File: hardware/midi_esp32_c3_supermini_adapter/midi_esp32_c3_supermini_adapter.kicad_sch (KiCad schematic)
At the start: 0 parts

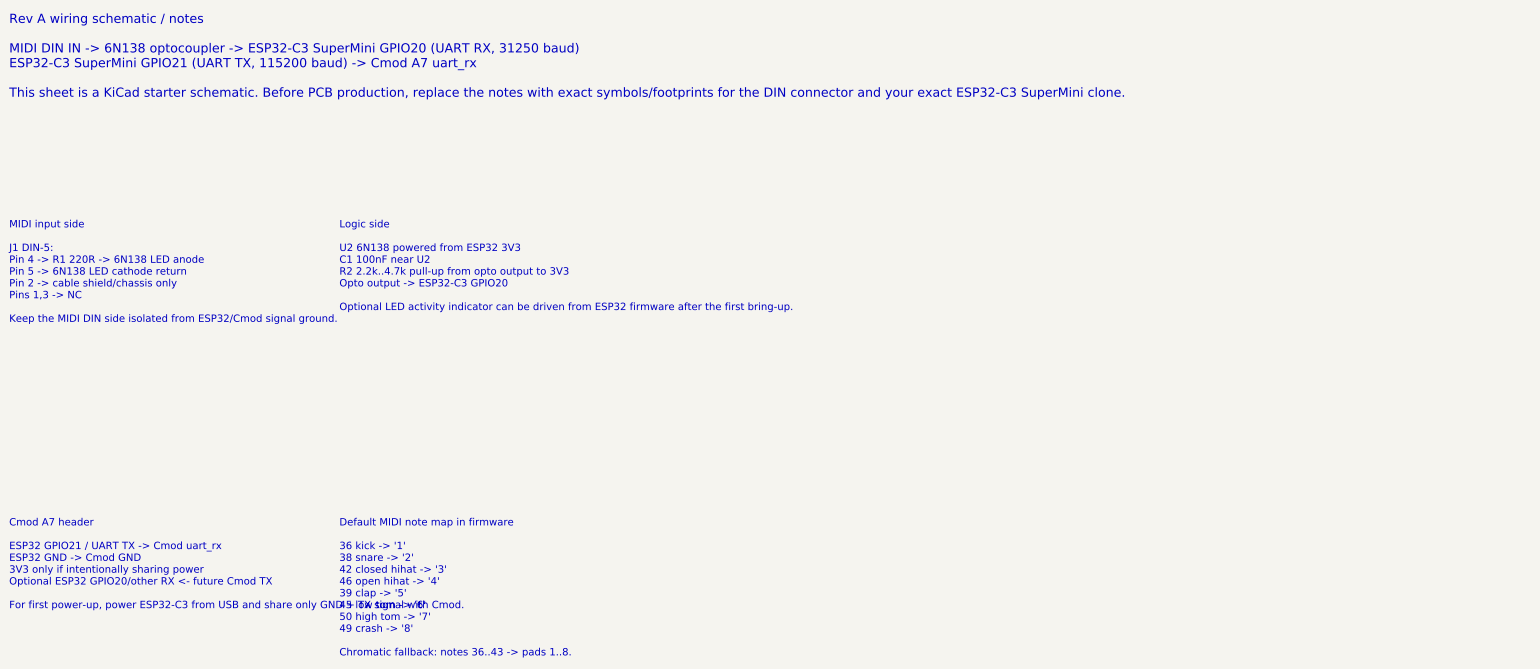
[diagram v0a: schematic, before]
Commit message: Replace MIDI adapter notes with schematic
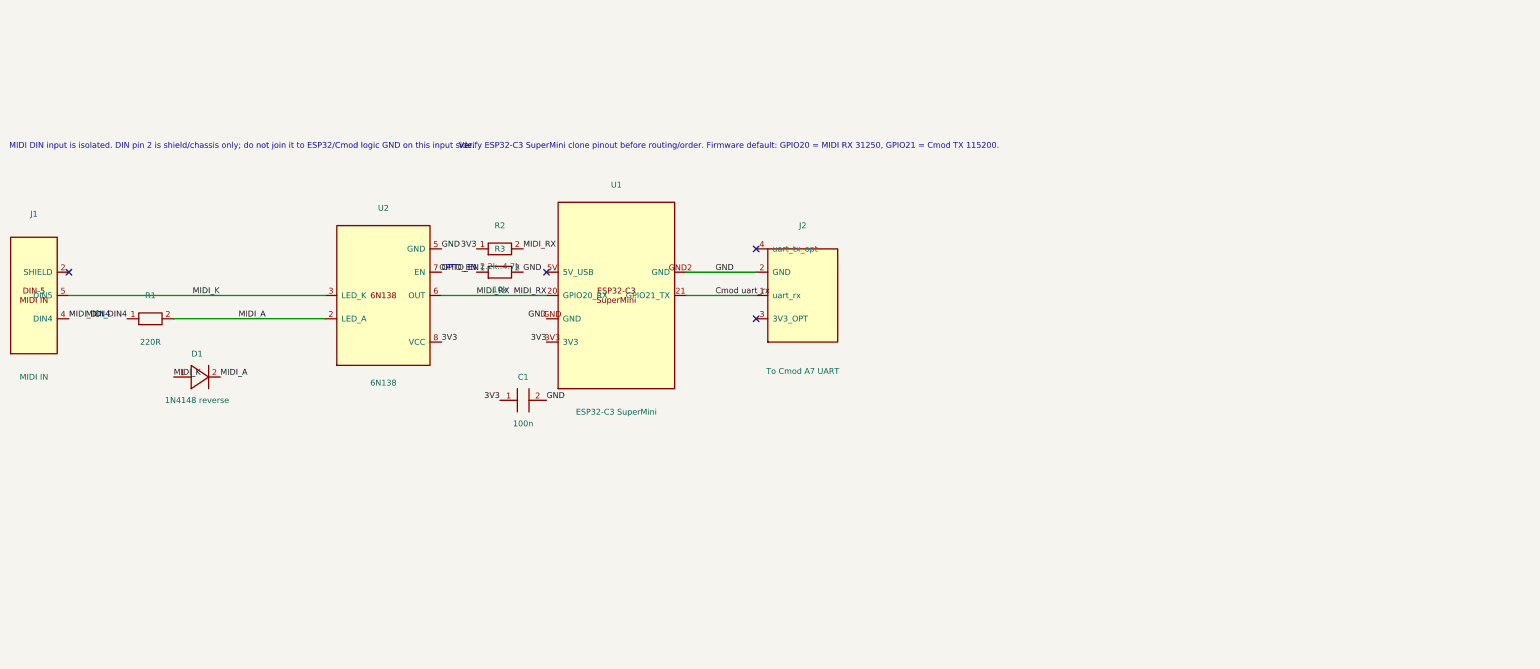
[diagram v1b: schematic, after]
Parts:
- added C1: 100n, symbol Adapter:CAP
- added D1: 1N4148 reverse, symbol Adapter:DIODE
- added J1: MIDI IN, symbol Adapter:DIN5_MIDI_IN
- added J2: To Cmod A7 UART, symbol Adapter:CMOD_UART
- added R1: 220R, symbol Adapter:R
- added R2: 2.2k..4.7k, symbol Adapter:R
- added R3: 10k, symbol Adapter:R
- added U1: ESP32-C3 SuperMini, symbol Adapter:ESP32_C3_SUPERMINI
- added U2: 6N138, symbol Adapter:6N138_MIDI
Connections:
- new net 3V3: C1.1, R2.1, U1.3V3, U2.8 (VCC)
- new net Cmod uart_rx: J2.1 (uart_rx), U1.21 (GPIO21_TX)
- new net GND: C1.2, J2.2 (GND), R3.2, U1.GND, U1.GND2 (GND), U2.5 (GND)
- new net MIDI_A: D1.2 (K), R1.2, U2.2 (LED_A)
- new net MIDI_DIN4: J1.4 (DIN4), R1.1
- new net MIDI_K: D1.1 (A), J1.5 (DIN5), U2.3 (LED_K)
- new net MIDI_RX: R2.2, U1.20 (GPIO20_RX), U2.6 (OUT)
- new net OPTO_EN: R3.1, U2.7 (EN)
- no-connect marks 0 -> 4
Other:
- note added: "MIDI DIN input is isolated. DIN pin 2 is shield/chassis only; do not join it to ESP32/Cmod logic GND on this input side."
- note added: "Verify ESP32-C3 SuperMini clone pinout before routing/order. Firmware default: GPIO20 = MIDI RX 31250, GPIO21 = Cmod TX 115200."
- note removed: "Cmod A7 header ESP32 GPIO21 / UART TX -> Cmod uart_rx ESP32 GND -> Cmod GND 3V3 only if intentionally sharing power Optional ESP32 GPIO20/other RX <- future Cmod TX For first power-up, power ESP32-C3 from USB and share only GND + TX signal with Cmod."
- note removed: "Default MIDI note map in firmware 36 kick -> '1' 38 snare -> '2' 42 closed hihat -> '3' 46 open hihat -> '4' 39 clap -> '5' 45 low tom -> '6' 50 high tom -> '7' 49 crash -> '8' Chromatic fallback: notes 36..43 -> pads 1..8."
- note removed: "Logic side U2 6N138 powered from ESP32 3V3 C1 100nF near U2 R2 2.2k..4.7k pull-up from opto output to 3V3 Opto output -> ESP32-C3 GPIO20 Optional LED activity indicator can be driven from ESP32 firmware after the first bring-up."
- note removed: "MIDI input side J1 DIN-5: Pin 4 -> R1 220R -> 6N138 LED anode Pin 5 -> 6N138 LED cathode return Pin 2 -> cable shield/chassis only Pins 1,3 -> NC Keep the MIDI DIN side isolated from ESP32/Cmod signal ground."
- note removed: "Rev A wiring schematic / notes MIDI DIN IN -> 6N138 optocoupler -> ESP32-C3 SuperMini GPIO20 (UART RX, 31250 baud) ESP32-C3 SuperMini GPIO21 (UART TX, 115200 baud) -> Cmod A7 uart_rx This sheet is a KiCad starter schematic. Before PCB production, replace the notes with exact symbols/footprints for the DIN connector and your exact ESP32-C3 SuperMini clone."
